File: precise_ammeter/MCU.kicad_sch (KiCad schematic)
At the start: 22 parts, among them J4 Conn_ARM_JTAG_SWD_10, U11 STM32G431C6Tx, U12 USBLC6-2P6, Y1 8MHz

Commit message: adding OLED display
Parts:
- added J6: Conn_01x04_Socket, Connector_PinSocket_2.54mm:PinSocket_1x04_P2.54mm_Vertical, symbol Connector:Conn_01x04_Socket
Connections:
- net +3V3: now also J6.1 (Pin_1)
- net GND: now also J6.2 (Pin_2)
- new net SCK: J6.3 (Pin_3)
- new net SDA: J6.4 (Pin_4)
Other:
- note added: "EXT_OLED connector"

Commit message: idk
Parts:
- added C40: 1u, Capacitor_SMD:C_0805_2012Metric, symbol Device:C
- added R30, R31: 4k7, Resistor_SMD:R_0805_2012Metric_Pad1.20x1.40mm_HandSolder, symbol Device:R
- R5: footprint (none) -> Resistor_SMD:R_0805_2012Metric_Pad1.20x1.40mm_HandSolder
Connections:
- net SCK is gone; now on net SCL: J6.3 (Pin_3)
- net +3V3: now also C40.1, R30.2, R31.2
- net GND: now also C40.2
- net SDA: now also U11.44 (PB7), R31.1
- net SCL: now reaches U11.39 (PA15)
- net SCL: now also R30.1
- no-connect marks 29 -> 27
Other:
- moved on the sheet: D3, J6, R1

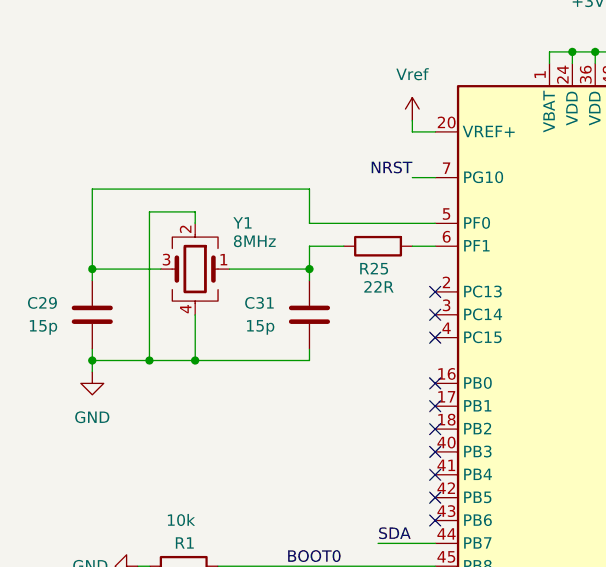
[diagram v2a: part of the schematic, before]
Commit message: Corrected all footprints before starting layout
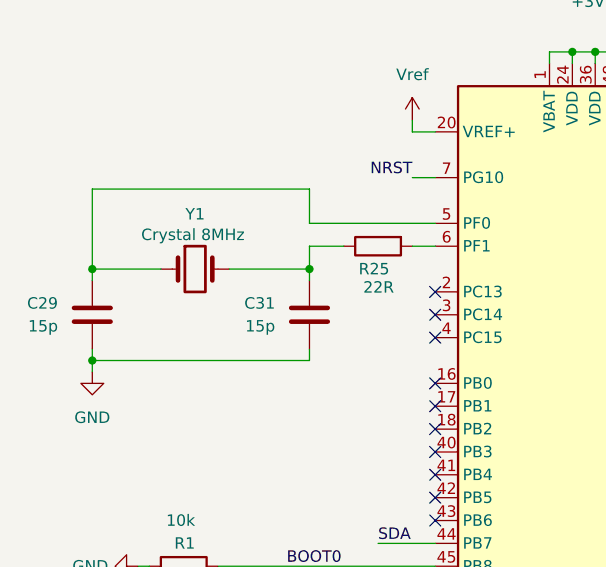
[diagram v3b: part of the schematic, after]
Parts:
- removed Y1: 8MHz, symbol Device:Crystal_GND24
- added Y1: Crystal 8MHz, Crystal:Crystal_SMD_HC49-SD, symbol Device:Crystal
- R1, R25: footprint (none) -> Resistor_SMD:R_0805_2012Metric_Pad1.20x1.40mm_HandSolder
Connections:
- net at C31.1, R25.1: now also Y1.2
- net at C29.1, U11.5 (PF0): now also Y1.1
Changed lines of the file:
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@@
 	)
 	(junction
-		(at 64.77 68.58)
-		(diameter 0)
-		(color 0 0 0 0)
-	)
-	(junction
 		(at 114.3 34.29)
 		(diameter 0)
@@
 	)
 	(junction
-		(at 58.42 58.42)
-		(diameter 0)
-		(color 0 0 0 0)
-	)
-	(junction
 		(at 111.76 148.59)
 		(diameter 0)
@@
 	)
 	(junction
-		(at 69.85 68.58)
+		(at 58.42 58.42)
 		(diameter 0)
 		(color 0 0 0 0)
@@
 	(wire
 		(pts
-			(xy 156.21 40.64) (xy 156.21 45.72)
+			(xy 73.66 58.42) (xy 82.55 58.42)
 		)
 		(stroke
@@
 	(wire
 		(pts
-			(xy 182.88 116.84) (xy 182.88 118.11)
+			(xy 156.21 40.64) (xy 156.21 45.72)
 		)
 		(stroke
@@
 	(wire
 		(pts
-			(xy 123.19 148.59) (xy 123.19 149.86)
+			(xy 182.88 116.84) (xy 182.88 118.11)
 		)
 		(stroke
@@
 	(wire
 		(pts
-			(xy 228.6 54.61) (xy 228.6 63.5)
+			(xy 123.19 148.59) (xy 123.19 149.86)
 		)
 		(stroke
@@
 	(wire
 		(pts
-			(xy 215.9 52.07) (xy 215.9 50.8)
+			(xy 228.6 54.61) (xy 228.6 63.5)
 		)
 		(stroke
@@
 	(wire
 		(pts
-			(xy 195.58 99.06) (xy 198.12 99.06)
+			(xy 215.9 52.07) (xy 215.9 50.8)
 		)
 		(stroke
@@
 	(wire
 		(pts
-			(xy 69.85 52.07) (xy 64.77 52.07)
+			(xy 195.58 99.06) (xy 198.12 99.06)
 		)
 		(stroke
@@
 	(wire
 		(pts
-			(xy 58.42 58.42) (xy 58.42 59.69)
-		)
-		(stroke
-			(width 0)
-			(type default)
-		)
-	)
-	(wire
-		(pts
 			(xy 182.88 85.09) (xy 182.88 86.36)
 		)
@@
 	(wire
 		(pts
+			(xy 58.42 58.42) (xy 66.04 58.42)
+		)
+		(stroke
+			(width 0)
+			(type default)
+		)
+	)
+	(wire
+		(pts
 			(xy 182.88 118.11) (xy 182.88 119.38)
 		)
@@
 	(wire
 		(pts
+			(xy 58.42 58.42) (xy 58.42 59.69)
+		)
+		(stroke
+			(width 0)
+			(type default)
+		)
+	)
+	(wire
+		(pts
 			(xy 119.38 33.02) (xy 119.38 35.56)
 		)
@@
 	(wire
 		(pts
-			(xy 82.55 58.42) (xy 73.66 58.42)
-		)
-		(stroke
-			(width 0)
-			(type default)
-		)
-	)
-	(wire
-		(pts
-			(xy 69.85 68.58) (xy 64.77 68.58)
-		)
-		(stroke
-			(width 0)
-			(type default)
-		)
-	)
-	(wire
-		(pts
-			(xy 66.04 58.42) (xy 58.42 58.42)
+			(xy 58.42 68.58) (xy 82.55 68.58)
 		)
 		(stroke
@@
 	(wire
 		(pts
-			(xy 69.85 53.34) (xy 69.85 52.07)
-		)
-		(stroke
-			(width 0)
-			(type default)
-		)
-	)
-	(wire
-		(pts
 			(xy 187.96 55.88) (xy 187.96 60.96)
 		)
@@
 	(wire
 		(pts
-			(xy 64.77 68.58) (xy 58.42 68.58)
-		)
-		(stroke
-			(width 0)
-			(type default)
-		)
-	)
-	(wire
-		(pts
-			(xy 69.85 63.5) (xy 69.85 68.58)
-		)
-		(stroke
-			(width 0)
-			(type default)
-		)
-	)
-	(wire
-		(pts
 			(xy 187.96 60.96) (xy 189.23 60.96)
 		)
@@
 	(wire
 		(pts
-			(xy 82.55 68.58) (xy 69.85 68.58)
-		)
-		(stroke
-			(width 0)
-			(type default)
-		)
-	)
-	(wire
-		(pts
 			(xy 215.9 60.96) (xy 215.9 63.5)
 		)
@@
 	(wire
 		(pts
-			(xy 64.77 52.07) (xy 64.77 68.58)
-		)
-		(stroke
-			(width 0)
-			(type default)
-		)
-	)
-	(wire
-		(pts
 			(xy 88.9 138.43) (xy 88.9 139.7)
 		)
@@
 	)
 	(symbol
-		(lib_id "Device:Crystal_GND24")
-		(at 69.85 58.42 0)
-		(mirror y)
-		(unit 1)
-		(exclude_from_sim no)
-		(in_bom yes)
-		(on_board yes)
-		(dnp no)
-		(property "Reference" "Y1"
-			(at 75.184 53.34 0)
-			(effects
-				(font
-					(size 1.27 1.27)
-				)
-			)
-		)
-		(property "Value" "8MHz"
-			(at 76.454 55.372 0)
-			(effects
-				(font
-					(size 1.27 1.27)
-				)
-			)
-		)
-		(property "Footprint" ""
-			(at 69.85 58.42 0)
-			(effects
-				(font
-					(size 1.27 1.27)
-				)
-				(hide yes)
-			)
-		)
-		(property "Datasheet" "~"
-			(at 69.85 58.42 0)
-			(effects
-				(font
-					(size 1.27 1.27)
-				)
-				(hide yes)
-			)
-		)
-		(property "Description" "Four pin crystal, GND on pins 2 and 4"
-			(at 69.85 58.42 0)
-			(effects
-				(font
-					(size 1.27 1.27)
-				)
-				(hide yes)
-			)
-		)
-		(pin "2"
-		)
-		(pin "3"
-		)
-		(pin "4"
-		)
-		(pin "1"
-		)
-		(instances
-			(project ""
-				(path "/0a62794b-916b-4c59-bf6a-35bad9d18073"
-					(reference "Y1")
-					(unit 1)
-				)
-			)
-			(project "precise_ammeter"
-				(path "/7da3b652-85ac-4caa-8d8d-9cad461e9c85/375ae359-eeb3-4ece-be83-a6d2731656da"
-					(reference "Y1")
-					(unit 1)
-				)
-			)
-		)
-	)
-	(symbol
 		(lib_id "Device:R")
 		(at 68.58 91.44 90)
@@
 			)
 		)
-		(property "Footprint" ""
+		(property "Footprint" "Resistor_SMD:R_0805_2012Metric_Pad1.20x1.40mm_HandSolder"
 			(at 68.58 93.218 90)
 			(effects
@@
 			)
 		)
-		(property "Footprint" ""
+		(property "Footprint" "Resistor_SMD:R_0805_2012Metric_Pad1.20x1.40mm_HandSolder"
 			(at 90.17 54.102 90)
 			(effects
@@
 					(unit 1)
 				)
+			)
+		)
+	)
+	(symbol
+		(lib_id "Device:Crystal")
+		(at 69.85 58.42 0)
+		(unit 1)
+		(exclude_from_sim no)
+		(in_bom yes)
+		(on_board yes)
+		(dnp no)
+		(property "Reference" "Y1"
+			(at 69.85 52.324 0)
+			(effects
+				(font
+					(size 1.27 1.27)
+				)
+			)
+		)
+		(property "Value" "Crystal 8MHz"
+			(at 69.596 54.61 0)
+			(effects
+				(font
+					(size 1.27 1.27)
+				)
+			)
+		)
+		(property "Footprint" "Crystal:Crystal_SMD_HC49-SD"
+			(at 69.85 58.42 0)
+			(effects
+				(font
+					(size 1.27 1.27)
+				)
+				(hide yes)
+			)
+		)
+		(property "Datasheet" "~"
+			(at 69.85 58.42 0)
+			(effects
+				(font
+					(size 1.27 1.27)
+				)
+				(hide yes)
+			)
+		)
+		(property "Description" "Two pin crystal"
+			(at 69.85 58.42 0)
+			(effects
+				(font
+					(size 1.27 1.27)
+				)
+				(hide yes)
+			)
+		)
+		(pin "2"
+		)
+		(pin "1"
+		)
+		(instances
+			(project ""
+				(path "/7da3b652-85ac-4caa-8d8d-9cad461e9c85/375ae359-eeb3-4ece-be83-a6d2731656da"
+					(reference "Y1")
+					(unit 1)
+				)

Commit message: USB layout
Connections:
- net at U11.33 (PA11): now also U12.3 (I/O2); no longer U12.1 (I/O1)
- net at U11.34 (PA12): now also U12.1 (I/O1); no longer U12.3 (I/O2)
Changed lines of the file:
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@@
+	(wire
+		(pts
+			(xy 138.43 72.39) (xy 138.43 71.12)
+		)
+		(stroke
+			(width 0)
+			(type default)
+		)
+	)
 	(wire
 		(pts
@@
 	(wire
 		(pts
+			(xy 142.24 73.66) (xy 134.62 73.66)
+		)
+		(stroke
+			(width 0)
+			(type default)
+		)
+	)
+	(wire
+		(pts
 			(xy 228.6 63.5) (xy 228.6 66.04)
 		)
@@
 	(wire
 		(pts
+			(xy 134.62 71.12) (xy 132.08 71.12)
+		)
+		(stroke
+			(width 0)
+			(type default)
+		)
+	)
+	(wire
+		(pts
 			(xy 182.88 85.09) (xy 182.88 86.36)
 		)
@@
 	(wire
 		(pts
+			(xy 134.62 73.66) (xy 134.62 71.12)
+		)
+		(stroke
+			(width 0)
+			(type default)
+		)
+	)
+	(wire
+		(pts
 			(xy 195.58 93.98) (xy 198.12 93.98)
 		)
@@
 	(wire
 		(pts
+			(xy 138.43 71.12) (xy 142.24 71.12)
+		)
+		(stroke
+			(width 0)
+			(type default)
+		)
+	)
+	(wire
+		(pts
 			(xy 82.55 59.69) (xy 82.55 58.42)
 		)
@@
 	(wire
 		(pts
-			(xy 132.08 71.12) (xy 142.24 71.12)
+			(xy 132.08 73.66) (xy 133.35 73.66)
 		)
 		(stroke
@@
 	(wire
 		(pts
-			(xy 132.08 73.66) (xy 142.24 73.66)
-		)
-		(stroke
-			(width 0)
-			(type default)
-		)
-	)
-	(wire
-		(pts
 			(xy 82.55 67.31) (xy 82.55 68.58)
 		)
@@
 	(wire
 		(pts
+			(xy 133.35 73.66) (xy 133.35 72.39)
+		)
+		(stroke
+			(width 0)
+			(type default)
+		)
+	)
+	(wire
+		(pts
 			(xy 93.98 43.18) (xy 96.52 43.18)
 		)
@@
 		)
 		(stroke
+			(width 0)
+			(type default)
+		)
+	)
+	(wire
+		(pts
+			(xy 133.35 72.39) (xy 138.43 72.39)
+		)
+		(stroke
